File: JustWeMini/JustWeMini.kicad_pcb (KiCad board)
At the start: 4 copper layers, 70 x 60 mm, 145 parts, among them J1 Conn_01x06, J2 Conn_01x02, J3 Conn_01x02, J4 Conn_01x02, J5 Conn_01x02, Q1 SSM6L820R, Q2 SSM6L820R, Q3 -, U1 ESP32-PICO-D4, U10 PCA9557D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

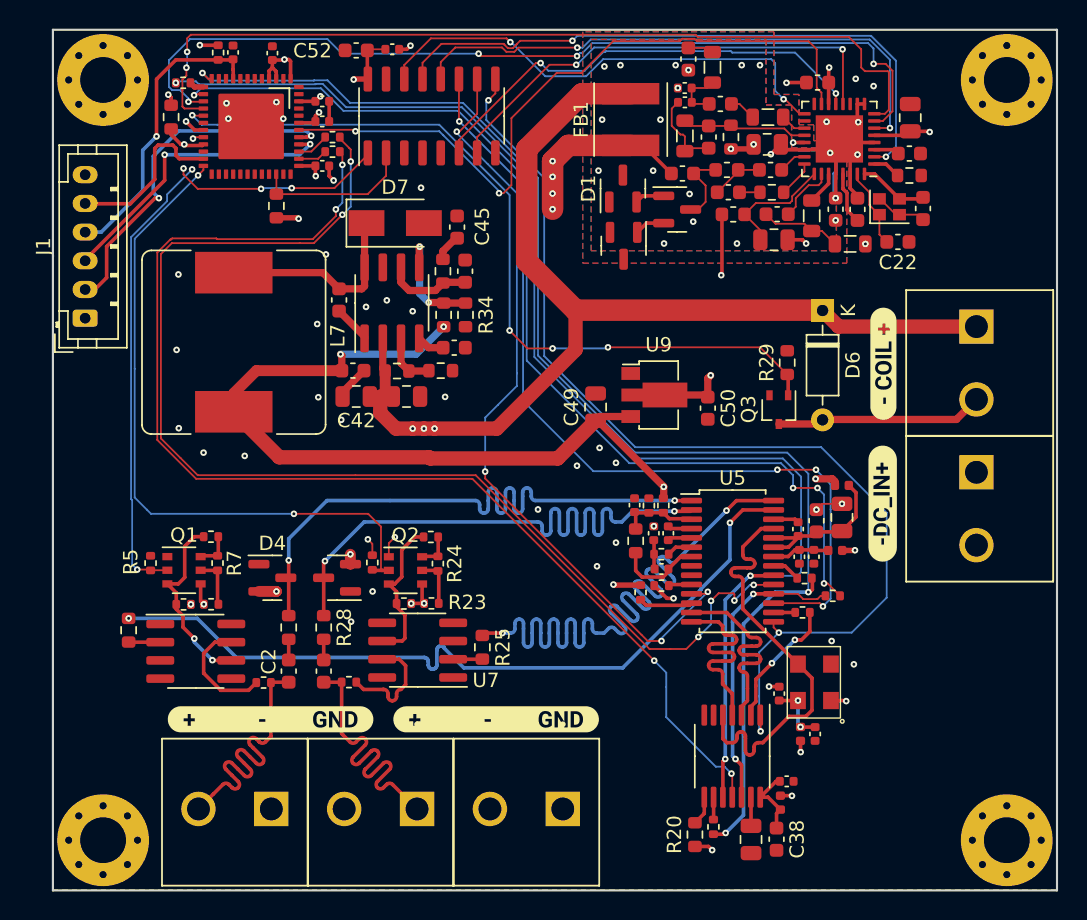
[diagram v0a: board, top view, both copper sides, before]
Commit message: Feat: minimal changes, added LED, fixed serigraphy
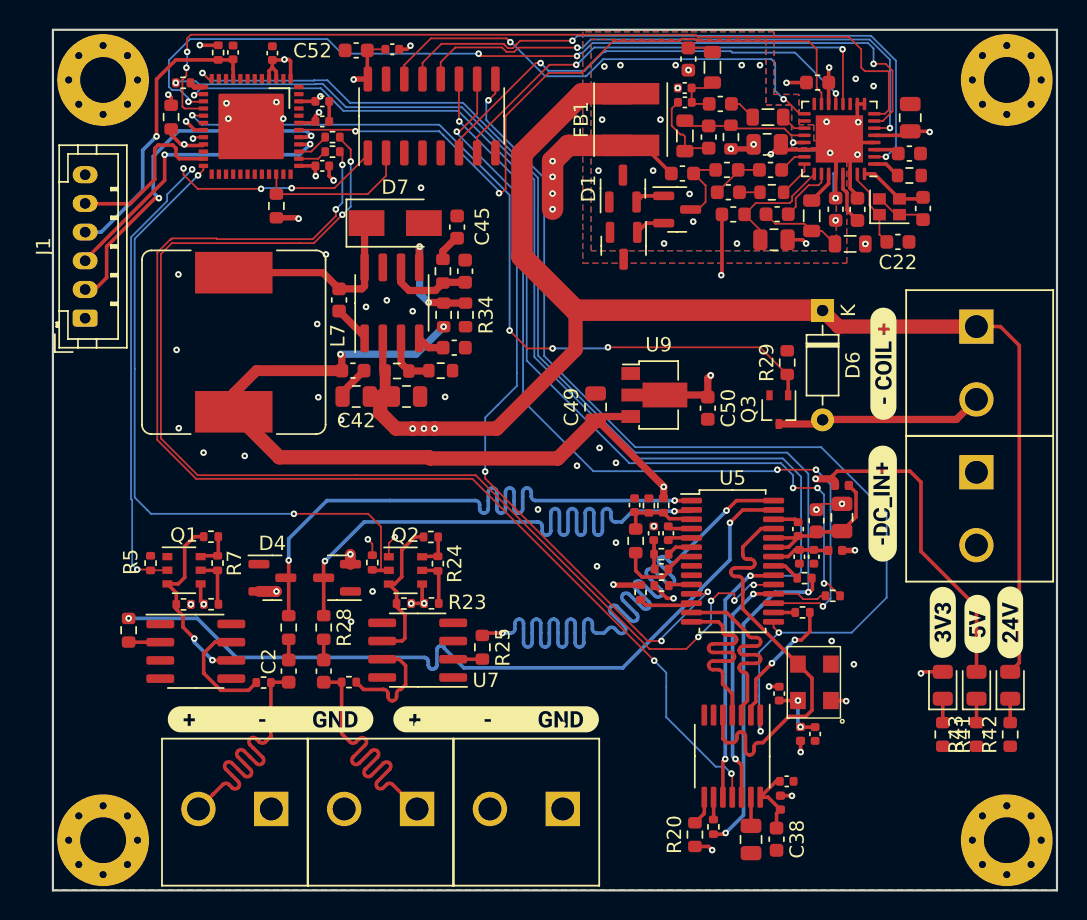
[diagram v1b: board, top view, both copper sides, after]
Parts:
- added D10: LED, LED_SMD:LED_0805_2012Metric, F.Cu at (123.9, 76.5)
- added D8: LED, LED_SMD:LED_0805_2012Metric, F.Cu at (121.5, 76.5)
- added D9: LED, LED_SMD:LED_0805_2012Metric, F.Cu at (126.2, 76.5)
- added R41: 120, Resistor_SMD:R_0603_1608Metric, F.Cu at (121.5, 79.9)
- added R42: 2k, Resistor_SMD:R_0603_1608Metric, F.Cu at (126.2, 79.9)
- added R43: 300, Resistor_SMD:R_0603_1608Metric, F.Cu at (123.9, 79.9)
- added kibuzzard-63FCB359: G***, kibuzzard-63FCB359, F.Cu at (121.5, 72.1)
- added kibuzzard-63FCB372: G***, kibuzzard-63FCB372, F.Cu at (124.0, 72.2)
- added kibuzzard-63FCB37D: G***, kibuzzard-63FCB37D, F.Cu at (126.2, 72.1)
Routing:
- net /24VDC: track 118.9 -> 145.7 mm
- net +5V: track 103.1 -> 124.8 mm
- net Net-(D9-Pad1): track 0.00 -> 1.67 mm
- net Net-(D8-Pad1): track 0.00 -> 1.67 mm
- net Net-(D10-Pad1): track 0.00 -> 1.67 mm
- net +3V3: track 44.3 -> 45.8 mm, vias 19 -> 20

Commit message: feat: Adjust silkscreen and board edgecut
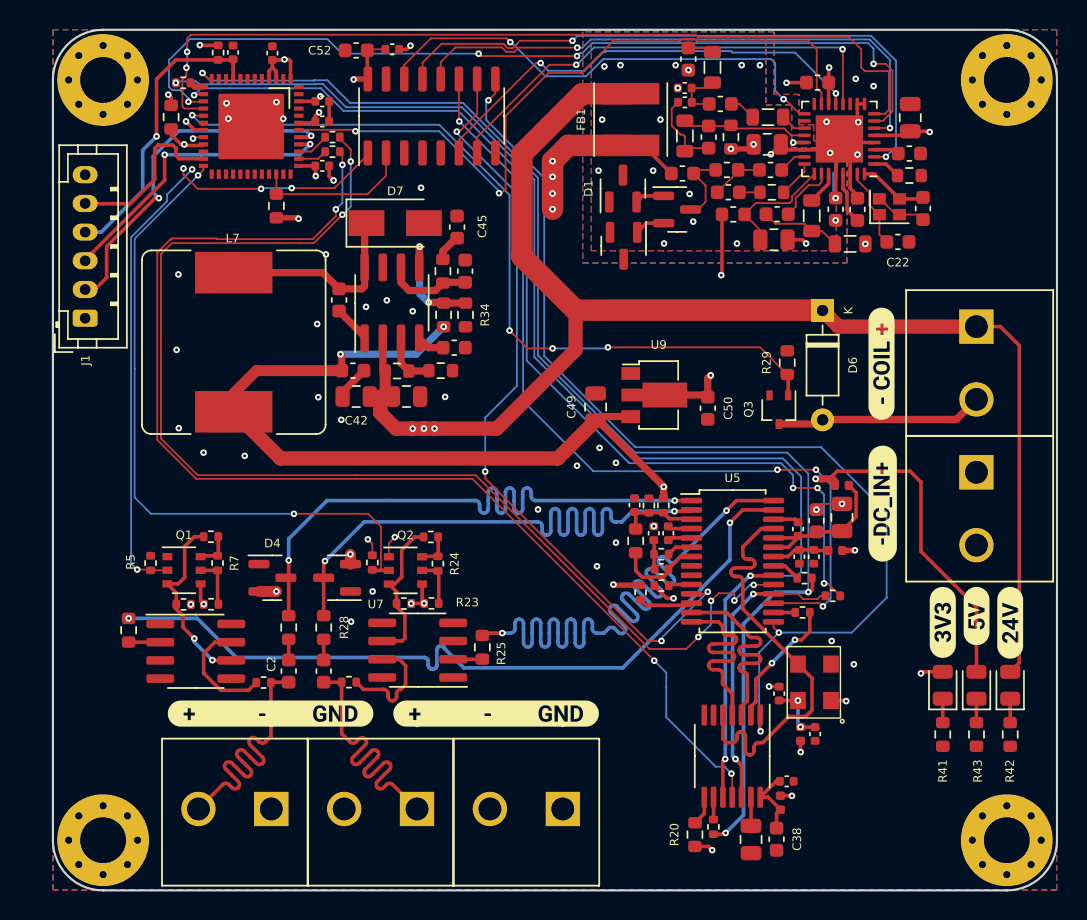
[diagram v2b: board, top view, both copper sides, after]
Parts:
- moved kibuzzard-63FCB372 0.55 mm to (123.9, 71.7)
- moved kibuzzard-63F90A85 0.40 mm to (74.7, 78.5)
- moved kibuzzard-63F90A85 0.40 mm to (90.4, 78.5)
- moved kibuzzard-63F8DB3C 0.13 mm to (117.3, 54.1)
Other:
- outline, holes or cut-outs redrawn
